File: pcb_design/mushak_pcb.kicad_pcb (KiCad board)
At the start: 2 copper layers, 57.7 x 40 mm, 118 parts, among them J1 Conn_01x04_Male, J10 IR_1, J11 AS5600_1, J12 IR_2, J13 AS5600_2, J14 IR_3, J15 ToF, J16 IR_4, J17 ToF, J2 Conn_01x02_Female, J3 BLE_Conn, J4 AS5600_Left, J5 AS5600_Right, J6 IR_1, J7 IR_3, J8 IR_2, J9 IR_4, M1 motor, M2 motor, Q1 DMN3065LW-7, Q2 DMN3065LW-7, Q3 DMN3065LW-7, Q4 DMN3065LW-7, Q5 DMN3065LW-7, SW1 SW_Push, SW2 SW_Push, U1 BA30BC0FP-E2, U2 AS5048B-HTSP, U3 DRV8833PW, U4 VL6180XV0NR/1, U5 MPU-6500, U6 STM32F405RGTx, U7 AS5048B-HTSP, Y1 25Mhz, Y2 32.769kHz

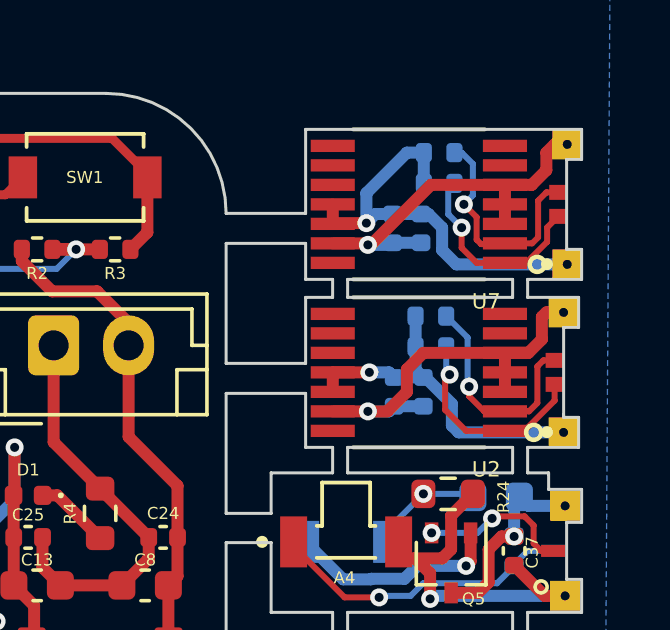
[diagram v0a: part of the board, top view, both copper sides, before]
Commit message: modified capacitors for encoders
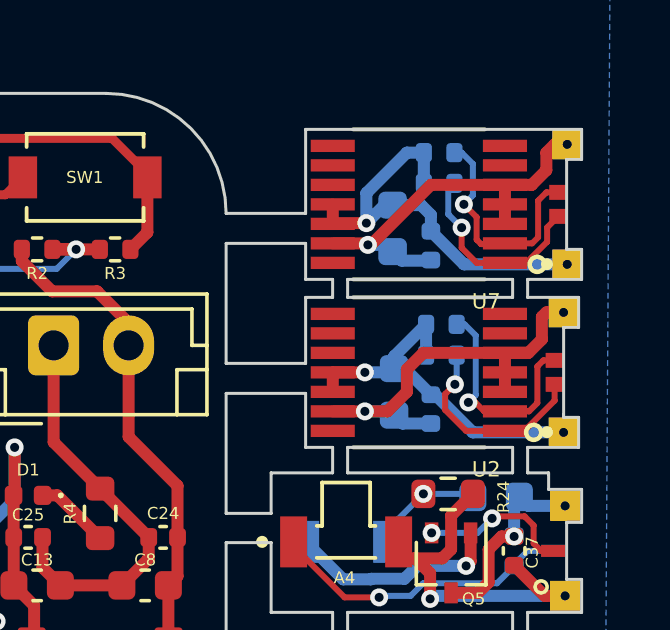
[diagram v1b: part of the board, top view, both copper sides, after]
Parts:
- C22, C23: value 0.1uF -> 10uF; footprint Capacitor_SMD:C_0402_1005Metric -> Capacitor_SMD:C_0603_1608Metric
- moved C41 0.66 mm to (200.8, 82.1)
- moved C40 0.63 mm to (200.8, 87.5)
- moved R5 0.45 mm to (201.2, 84.7)
- moved R8 0.45 mm to (201.2, 85.7)
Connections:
- net /AS5600_Left/+3V0_s renamed /AS5048_Left/+3V0_s
- net /AS5600_Left/GND_s renamed /AS5048_Left/GND_s
- net /AS5600_Left/SCL_s renamed /AS5048_Left/SCL_s
- net /AS5600_Left/SDA_s renamed /AS5048_Left/SDA_s
- net /AS5600_Right/+3V0_s renamed /AS5048_Right/+3V0_s
- net /AS5600_Right/GND_s renamed /AS5048_Right/GND_s
- net /AS5600_Right/SCL_s renamed /AS5048_Right/SCL_s
- net /AS5600_Right/SDA_s renamed /AS5048_Right/SDA_s
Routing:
- net /AS5048_Right/GND_s: track 12.7 -> 13.2 mm

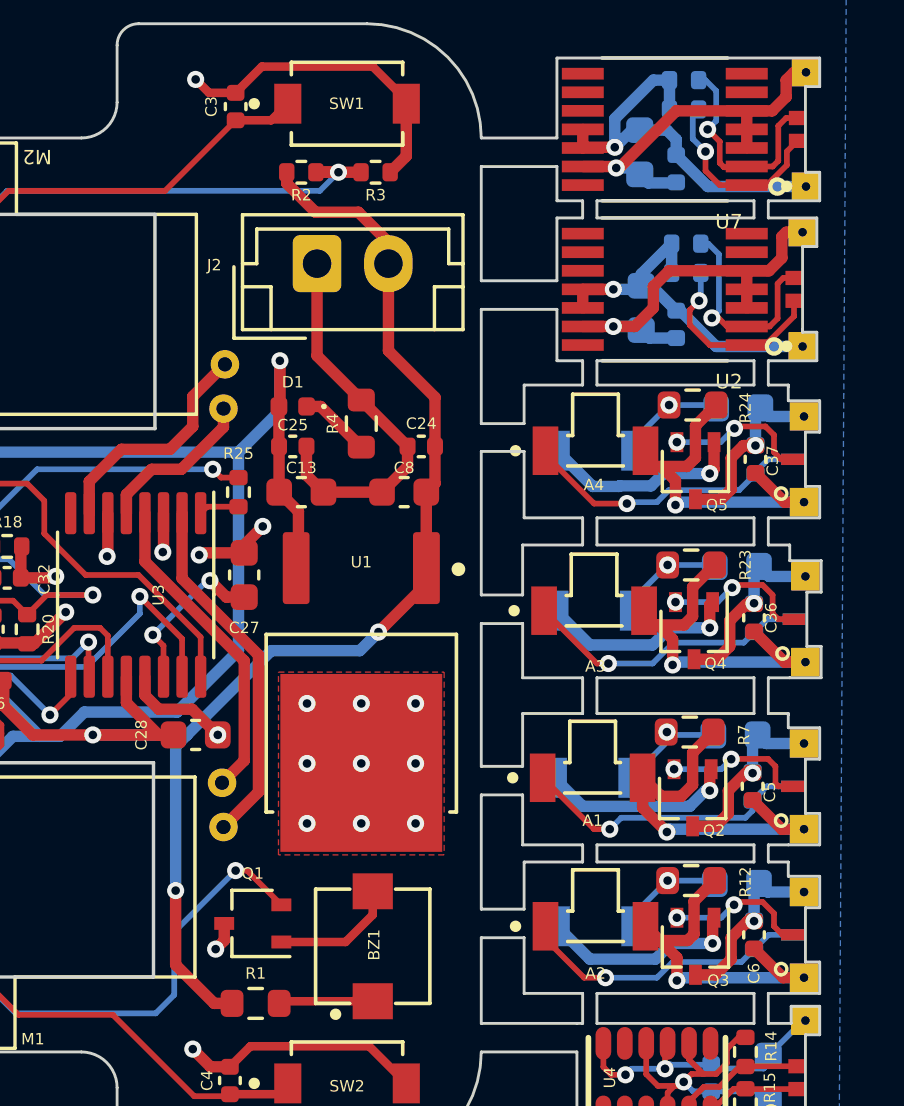
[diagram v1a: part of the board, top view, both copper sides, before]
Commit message: Add resistors between MOSFET gate
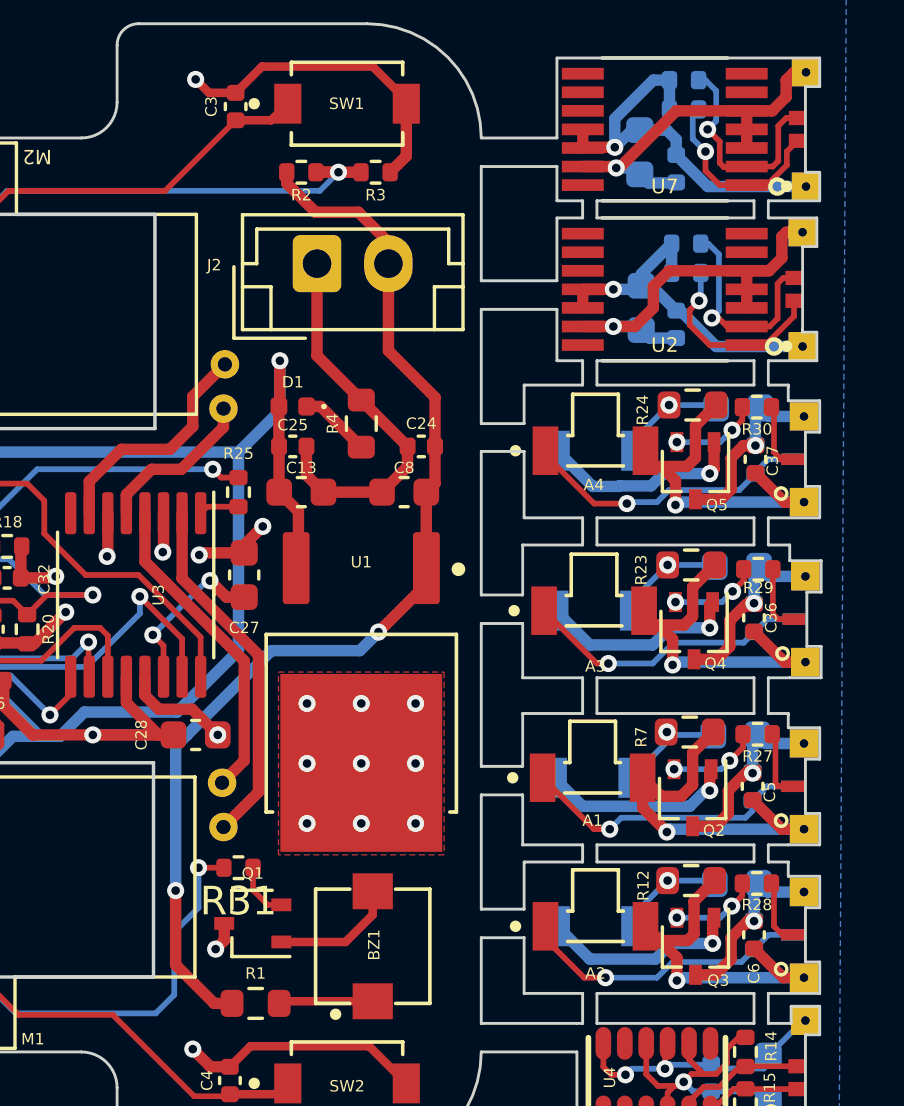
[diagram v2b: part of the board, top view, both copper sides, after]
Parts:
- added R27: 150, Resistor_SMD:R_0402_1005Metric, F.Cu at (203.7, 101.9)
- added R28: 150, Resistor_SMD:R_0402_1005Metric, F.Cu at (203.7, 107.1)
- added R29: 150, Resistor_SMD:R_0402_1005Metric, F.Cu at (203.7, 96.1)
- added R30: 150, Resistor_SMD:R_0402_1005Metric, F.Cu at (203.7, 90.4)
- added R31: 150, Resistor_SMD:R_0402_1005Metric, F.Cu at (185.5, 106.5)
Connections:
- Q1 pad 2: BUZZER_OP -> Net-(Q1-Pad2)
- Q2 pad 2: /IR_sensor/IR_POW_1 -> Net-(Q2-Pad2)
- Q3 pad 2: /IR_sensor/IR_POW_2 -> Net-(Q3-Pad2)
- Q4 pad 2: /IR_sensor/IR_POW_4 -> Net-(Q4-Pad2)
- Q5 pad 2: /IR_sensor/IR_POW_3 -> Net-(Q5-Pad2)
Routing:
- net Net-(Q2-Pad2): track 0.00 -> 3.19 mm, vias 0 -> 2
- net Net-(Q4-Pad2): track 0.00 -> 3.09 mm, vias 0 -> 2
- net Net-(Q5-Pad2): track 0.00 -> 3.06 mm, vias 0 -> 2
- net Net-(Q3-Pad2): track 0.00 -> 3.04 mm, vias 0 -> 2
- net /IR_sensor/IR_POW_4: track 5.28 -> 2.38 mm, vias 2 -> 0
- net /IR_sensor/IR_POW_3: track 5.11 -> 2.37 mm, vias 2 -> 0
- net /IR_sensor/IR_POW_2: track 5.02 -> 2.31 mm, vias 2 -> 0
- net /IR_sensor/IR_POW_1: track 5.05 -> 2.41 mm, vias 2 -> 0
- net Net-(Q1-Pad2): track 0.00 -> 1.99 mm
- net BUZZER_OP: track 48.0 -> 46.4 mm
